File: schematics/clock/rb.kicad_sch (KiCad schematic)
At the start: 19 parts, among them U10 74LS173, U11 74LS173, U12 74LS245

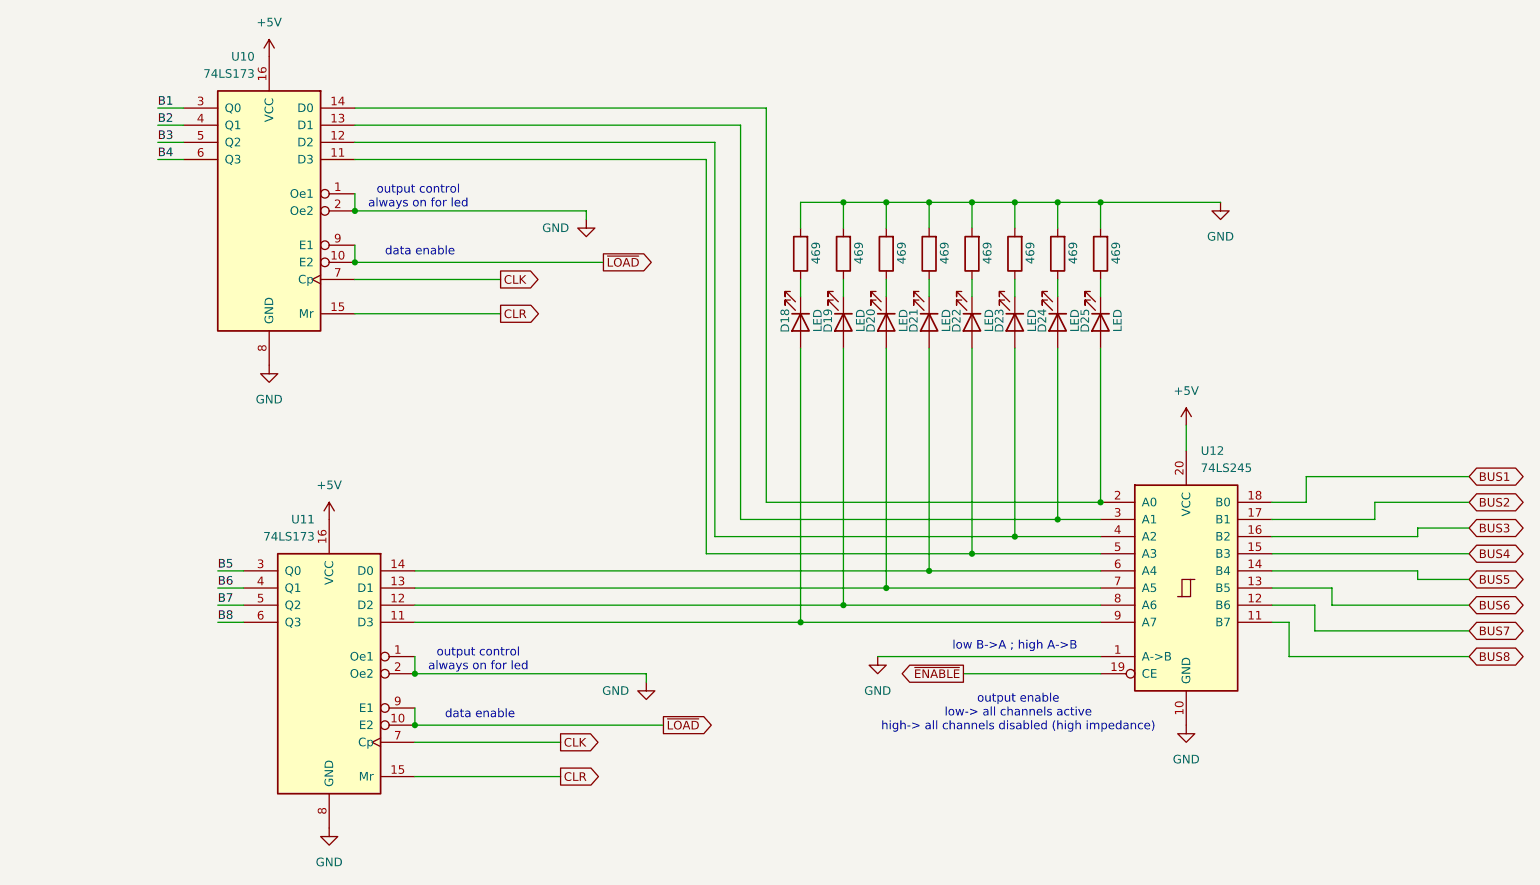
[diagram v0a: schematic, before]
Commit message: swap led position on registers
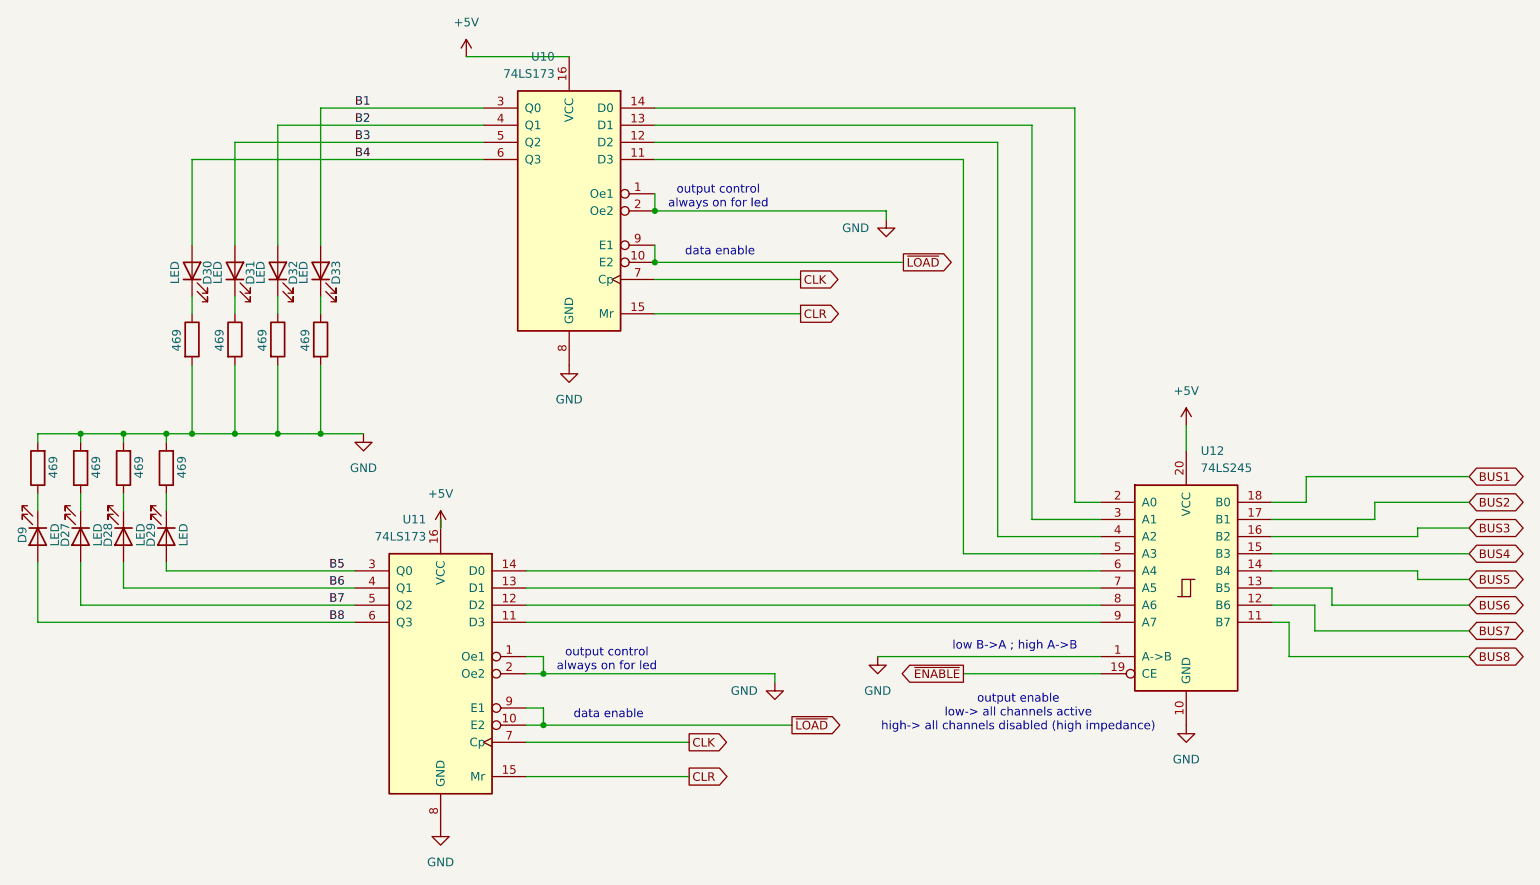
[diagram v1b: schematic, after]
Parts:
- removed D18, D19, D20, D21, D22, D23, D24, D25: LED, symbol Device:LED
- removed RLED25, RLED26, RLED27, RLED28, RLED29, RLED30, RLED31, RLED32: 469, symbol Device:R
- added D27, D28, D29, D30, D31, D32, D33, D9: LED, symbol Device:LED
- added RLED34, RLED35, RLED36, RLED37, RLED38, RLED39, RLED40, RLED8: 469, symbol Device:R
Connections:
- net B1: now also D33.2 (A)
- net B2: now also D32.2 (A)
- net B3: now also D31.2 (A)
- net B4: now also D30.2 (A)
- net B5: now also D29.2 (A)
- net B6: now also D28.2 (A)
- net B7: now also D27.2 (A)
- net B8: now also D9.2 (A)
- net GND: now also RLED34.2, RLED35.2, RLED36.2, RLED37.2, RLED38.2, RLED39.2, RLED40.2, RLED8.2
- new net: D29.1 (K), RLED36.1
- new net: D33.1 (K), RLED40.1
- new net: D31.1 (K), RLED38.1
- new net: D28.1 (K), RLED35.1
- new net: D30.1 (K), RLED37.1
- new net: D32.1 (K), RLED39.1
- new net: D9.1 (K), RLED8.1
- new net: D27.1 (K), RLED34.1
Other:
- moved on the sheet: U10, U11

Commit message: add alu
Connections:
- net CLR is gone; now on net GND: U10.15 (Mr), U11.15 (Mr)
- net ~{ENABLE} renamed enable
- net ~{LOAD} renamed load
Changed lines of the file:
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@@
 	(wire
 		(pts
-			(xy 102.87 144.78) (xy 127 144.78)
+			(xy 102.87 144.78) (xy 123.19 144.78)
 		)
 		(stroke
@@
 	(wire
 		(pts
-			(xy 109.22 38.1) (xy 93.98 38.1)
-		)
-		(stroke
-			(width 0)
-			(type default)
-		)
-	)
-	(wire
-		(pts
 			(xy 43.18 116.84) (xy 77.47 116.84)
 		)
@@
 			(width 0)
 			(type default)
+		)
+	)
+	(label "load"
+		(at 142.24 137.16 0)
+		(effects
+			(font
+				(size 1.27 1.27)
+			)
+			(justify left bottom)
 		)
 	)
@@
 		)
 	)
+	(label "enable"
+		(at 167.64 129.54 0)
+		(effects
+			(font
+				(size 1.27 1.27)
+			)
+			(justify left bottom)
+		)
+	)
+	(label "load"
+		(at 158.75 68.58 0)
+		(effects
+			(font
+				(size 1.27 1.27)
+			)
+			(justify left bottom)
+		)
+	)
 	(label "B1"
 		(at 77.47 45.72 0)
@@
 			)
 			(justify left bottom)
-		)
-	)
-	(global_label "~{ENABLE}"
-		(shape output)
-		(at 167.64 129.54 180)
-		(fields_autoplaced yes)
-		(effects
-			(font
-				(size 1.27 1.27)
-			)
-			(justify right)
-		)
-		(property "Intersheetrefs" "${INTERSHEET_REFS}"
-			(at 157.6396 129.54 0)
-			(effects
-				(font
-					(size 1.27 1.27)
-				)
-				(justify right)
-				(hide yes)
-			)
 		)
 	)
@@
 		)
 	)
-	(global_label "CLR"
-		(shape output)
-		(at 143.51 76.2 0)
-		(fields_autoplaced yes)
-		(effects
-			(font
-				(size 1.27 1.27)
-			)
-			(justify left)
-		)
-		(property "Intersheetrefs" "${INTERSHEET_REFS}"
-			(at 150.0633 76.2 0)
-			(effects
-				(font
-					(size 1.27 1.27)
-				)
-				(justify left)
-				(hide yes)
-			)
-		)
-	)
 	(global_label "BUS6"
 		(shape bidirectional)
@@
 		)
 	)
-	(global_label "CLR"
-		(shape output)
-		(at 127 144.78 0)
-		(fields_autoplaced yes)
-		(effects
-			(font
-				(size 1.27 1.27)
-			)
-			(justify left)
-		)
-		(property "Intersheetrefs" "${INTERSHEET_REFS}"
-			(at 133.5533 144.78 0)
-			(effects
-				(font
-					(size 1.27 1.27)
-				)
-				(justify left)
-				(hide yes)
-			)
-		)
-	)
-	(global_label "~{LOAD}"
-		(shape output)
-		(at 158.75 68.58 0)
-		(fields_autoplaced yes)
-		(effects
-			(font
-				(size 1.27 1.27)
-			)
-			(justify left)
-		)
-		(property "Intersheetrefs" "${INTERSHEET_REFS}"
-			(at 166.4524 68.58 0)
-			(effects
-				(font
-					(size 1.27 1.27)
-				)
-				(justify left)
-				(hide yes)
-			)
-		)
-	)
 	(global_label "CLK"
 		(shape output)
@@
 		(property "Intersheetrefs" "${INTERSHEET_REFS}"
 			(at 251.686 100.33 0)
-			(effects
-				(font
-					(size 1.27 1.27)
-				)
-				(justify left)
-				(hide yes)
-			)
-		)
-	)
-	(global_label "~{LOAD}"
-		(shape output)
-		(at 142.24 137.16 0)
-		(fields_autoplaced yes)
-		(effects
-			(font
-				(size 1.27 1.27)
-			)
-			(justify left)
-		)
-		(property "Intersheetrefs" "${INTERSHEET_REFS}"
-			(at 149.9424 137.16 0)
 			(effects
 				(font
@@
 	)
 	(symbol
+		(lib_id "power:GND")
+		(at 143.51 76.2 0)
+		(unit 1)
+		(exclude_from_sim no)
+		(in_bom yes)
+		(on_board yes)
+		(dnp no)
+		(fields_autoplaced yes)
+		(property "Reference" "#PWR049"
+			(at 143.51 82.55 0)
+			(effects
+				(font
+					(size 1.27 1.27)
+				)
+				(hide yes)
+			)
+		)
+		(property "Value" "GND"
+			(at 143.51 81.28 0)
+			(effects
+				(font
+					(size 1.27 1.27)
+				)
+			)
+		)
+		(property "Footprint" ""
+			(at 143.51 76.2 0)
+			(effects
+				(font
+					(size 1.27 1.27)
+				)
+				(hide yes)
+			)
+		)
+		(property "Datasheet" ""
+			(at 143.51 76.2 0)
+			(effects
+				(font
+					(size 1.27 1.27)
+				)
+				(hide yes)
+			)
+		)
+		(property "Description" "Power symbol creates a global label with name \"GND\" , ground"
+			(at 143.51 76.2 0)
+			(effects
+				(font
+					(size 1.27 1.27)
+				)
+				(hide yes)
+			)
+		)
+		(pin "1"
+		)
+		(instances
+			(project "clock"
+				(path "/1be175cd-1437-4d72-8152-541f02e1a99b/d58d7b4b-c7c9-4a9b-82e5-f70bb60ff1ca/af91bf73-a3ad-42a1-90ad-f08c489005c9"
+					(reference "#PWR049")
+					(unit 1)
+				)
+			)
+		)
+	)
+	(symbol
 		(lib_id "Device:R")
 		(at 66.04 80.01 0)
@@
 	)
 	(symbol
+		(lib_id "power:GND")
+		(at 123.19 144.78 0)
+		(unit 1)
+		(exclude_from_sim no)
+		(in_bom yes)
+		(on_board yes)
+		(dnp no)
+		(fields_autoplaced yes)
+		(property "Reference" "#PWR050"
+			(at 123.19 151.13 0)
+			(effects
+				(font
+					(size 1.27 1.27)
+				)
+				(hide yes)
+			)
+		)
+		(property "Value" "GND"
+			(at 123.19 149.86 0)
+			(effects
+				(font
+					(size 1.27 1.27)
+				)
+			)
+		)
+		(property "Footprint" ""
+			(at 123.19 144.78 0)
+			(effects
+				(font
+					(size 1.27 1.27)
+				)
+				(hide yes)
+			)
+		)
+		(property "Datasheet" ""
+			(at 123.19 144.78 0)
+			(effects
+				(font
+					(size 1.27 1.27)
+				)
+				(hide yes)
+			)
+		)
+		(property "Description" "Power symbol creates a global label with name \"GND\" , ground"
+			(at 123.19 144.78 0)
+			(effects
+				(font
+					(size 1.27 1.27)
+				)
+				(hide yes)
+			)
+		)
+		(pin "1"
+		)
+		(instances
+			(project "clock"
+				(path "/1be175cd-1437-4d72-8152-541f02e1a99b/d58d7b4b-c7c9-4a9b-82e5-f70bb60ff1ca/af91bf73-a3ad-42a1-90ad-f08c489005c9"
+					(reference "#PWR050")
+					(unit 1)
+				)
+			)
+		)
+	)
+	(symbol
 		(lib_id "74xx:74LS173")
 		(at 109.22 60.96 0)
@@
 	(symbol
 		(lib_id "power:+5V")
-		(at 93.98 38.1 0)
+		(at 109.22 38.1 0)
 		(unit 1)
 		(exclude_from_sim no)
@@
 		(fields_autoplaced yes)
 		(property "Reference" "#PWR023"
-			(at 93.98 41.91 0)
+			(at 109.22 41.91 0)
 			(effects
 				(font
@@
 		)
 		(property "Value" "+5V"
-			(at 93.98 33.02 0)
+			(at 109.22 33.02 0)
 			(effects
 				(font
@@
 		)
 		(property "Footprint" ""
-			(at 93.98 38.1 0)
+			(at 109.22 38.1 0)
 			(effects
 				(font
@@
 		)
 		(property "Datasheet" ""
-			(at 93.98 38.1 0)
+			(at 109.22 38.1 0)
 			(effects
 				(font
@@
 		)
 		(property "Description" "Power symbol creates a global label with name \"+5V\""
-			(at 93.98 38.1 0)
-			(effects
-				(font
+			(at 109.22 38.1 0)
+			(effects
+				(font

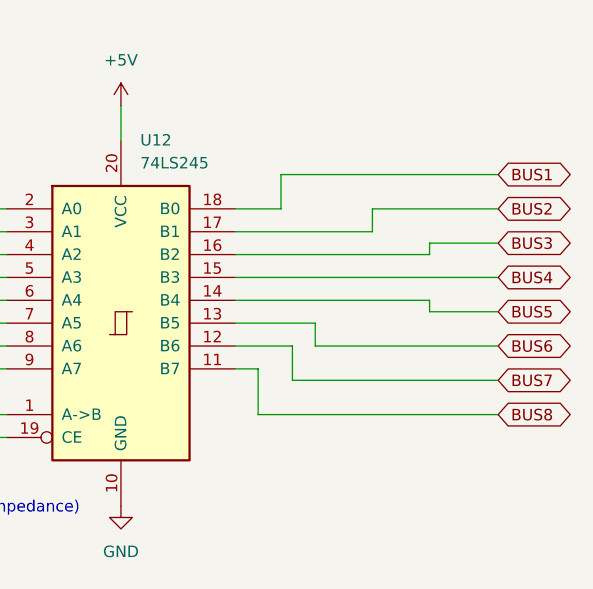
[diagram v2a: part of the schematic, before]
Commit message: add ram, change bus
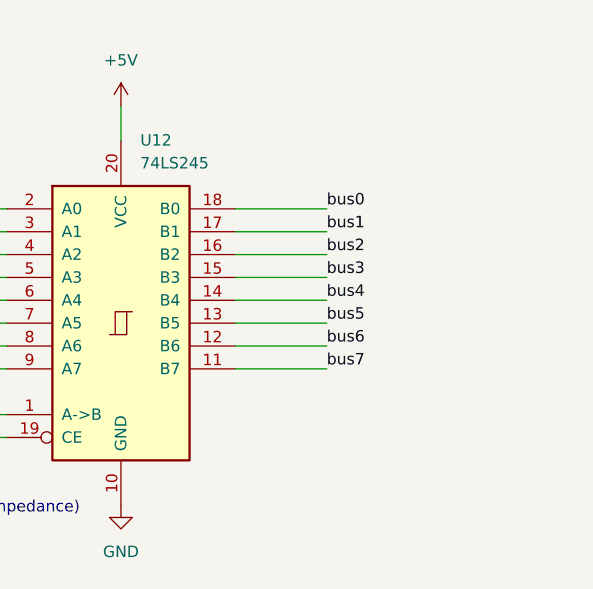
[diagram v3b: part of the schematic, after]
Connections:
- net BUS1 renamed bus0
- net BUS2 renamed bus1
- net BUS3 renamed bus2
- net BUS4 renamed bus3
- net BUS5 renamed bus4
- net BUS6 renamed bus5
- net BUS7 renamed bus6
- net BUS8 renamed bus7
